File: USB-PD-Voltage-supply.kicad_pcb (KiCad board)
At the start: 4 copper layers, 73.6 x 70.6 mm, 231 parts, among them J1 DC-005-5A-2.5-SMT, J2 Conn_01x07_Pin, J3 Conn_01x04_Pin, J4 TYPE-C-31-M-31, J5 Conn_01x11_Pin, J6 Conn_01x11_Pin, J7 Conn_01x11_Pin, Q1 STL6P3LLH6, Q2 STL6P3LLH6, SW1 TS-1088-AR02016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

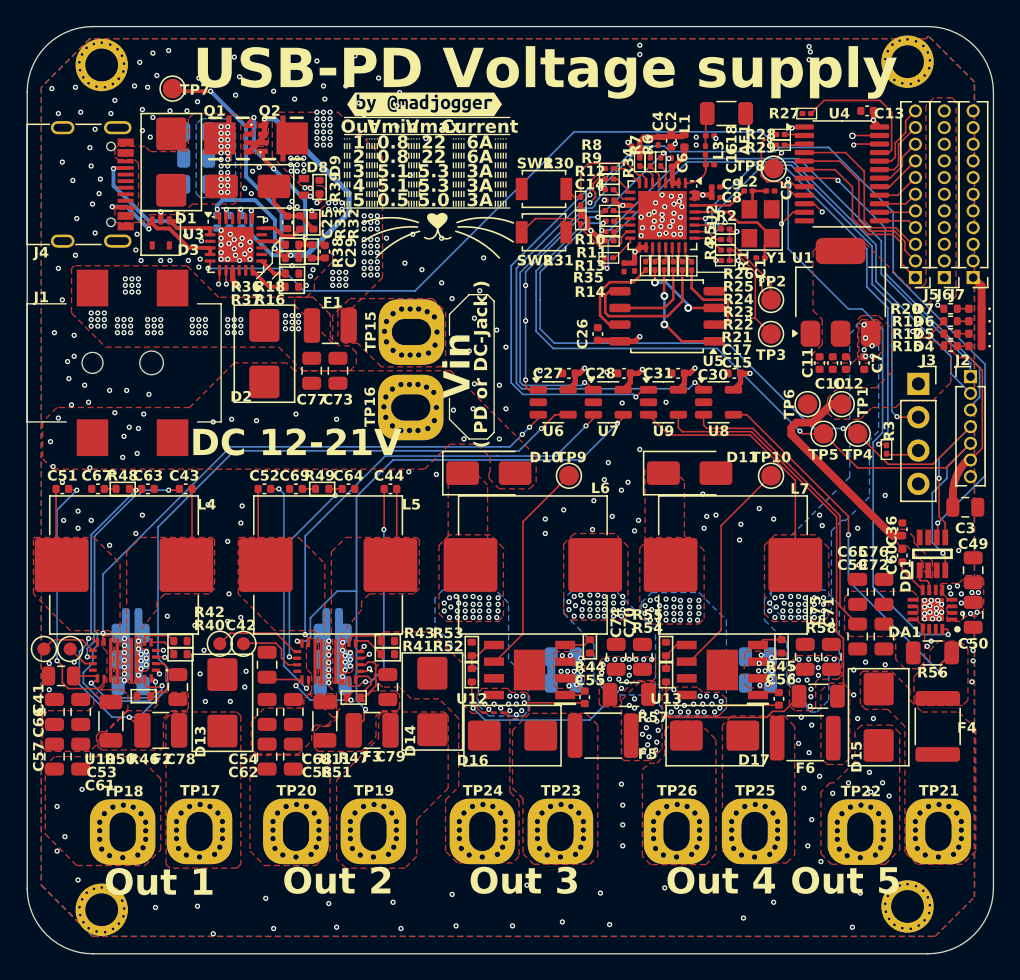
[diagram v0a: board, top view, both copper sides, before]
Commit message: PCB upd for DFM checking and manufacturing
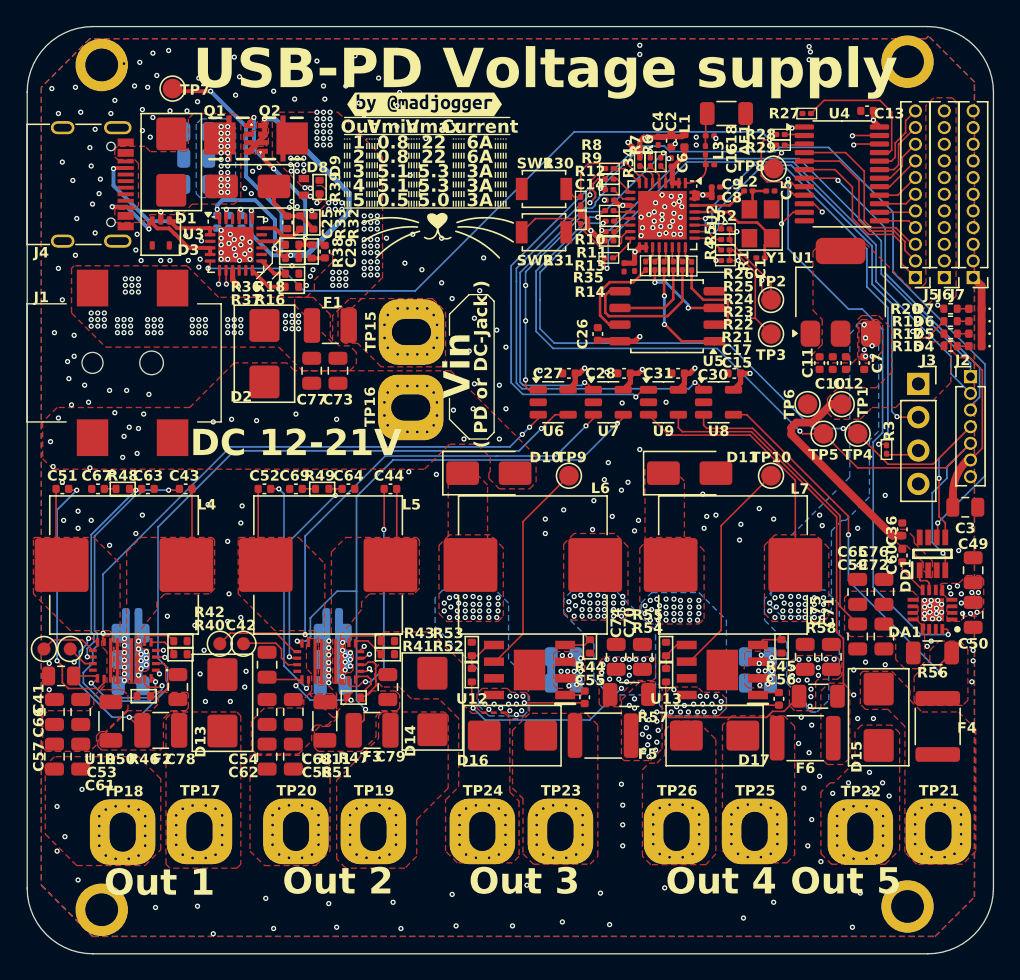
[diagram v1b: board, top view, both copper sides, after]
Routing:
- net Net-(F1-Pad2): vias 0 -> 16
- net Net-(D17-A): vias 0 -> 16
- net Net-(D16-A): vias 0 -> 16
- net Net-(D15-A): vias 0 -> 16
- net Net-(D14-A): vias 0 -> 16
- net Net-(D13-A): vias 0 -> 16
- net Earth: vias 400 -> 429
